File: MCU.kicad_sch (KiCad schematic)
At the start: 13 parts, among them J7 USB_C_Receptacle_USB2.0_16P, U1 STM32G474RCTx

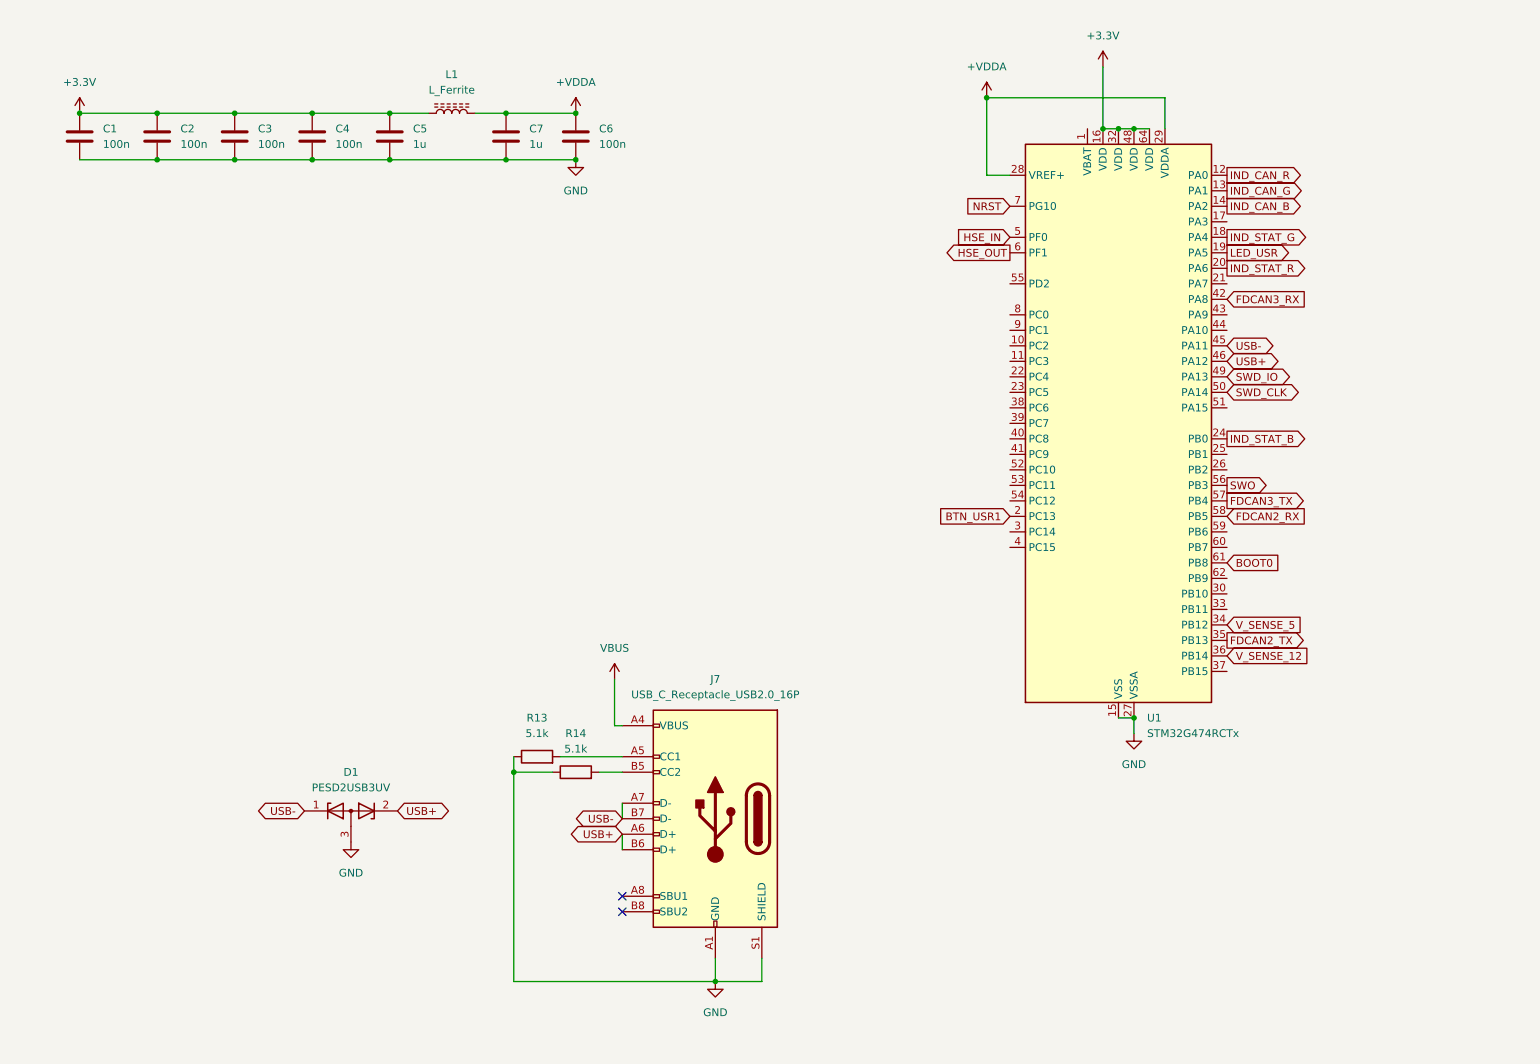
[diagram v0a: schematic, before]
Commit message: add power, some mcu components
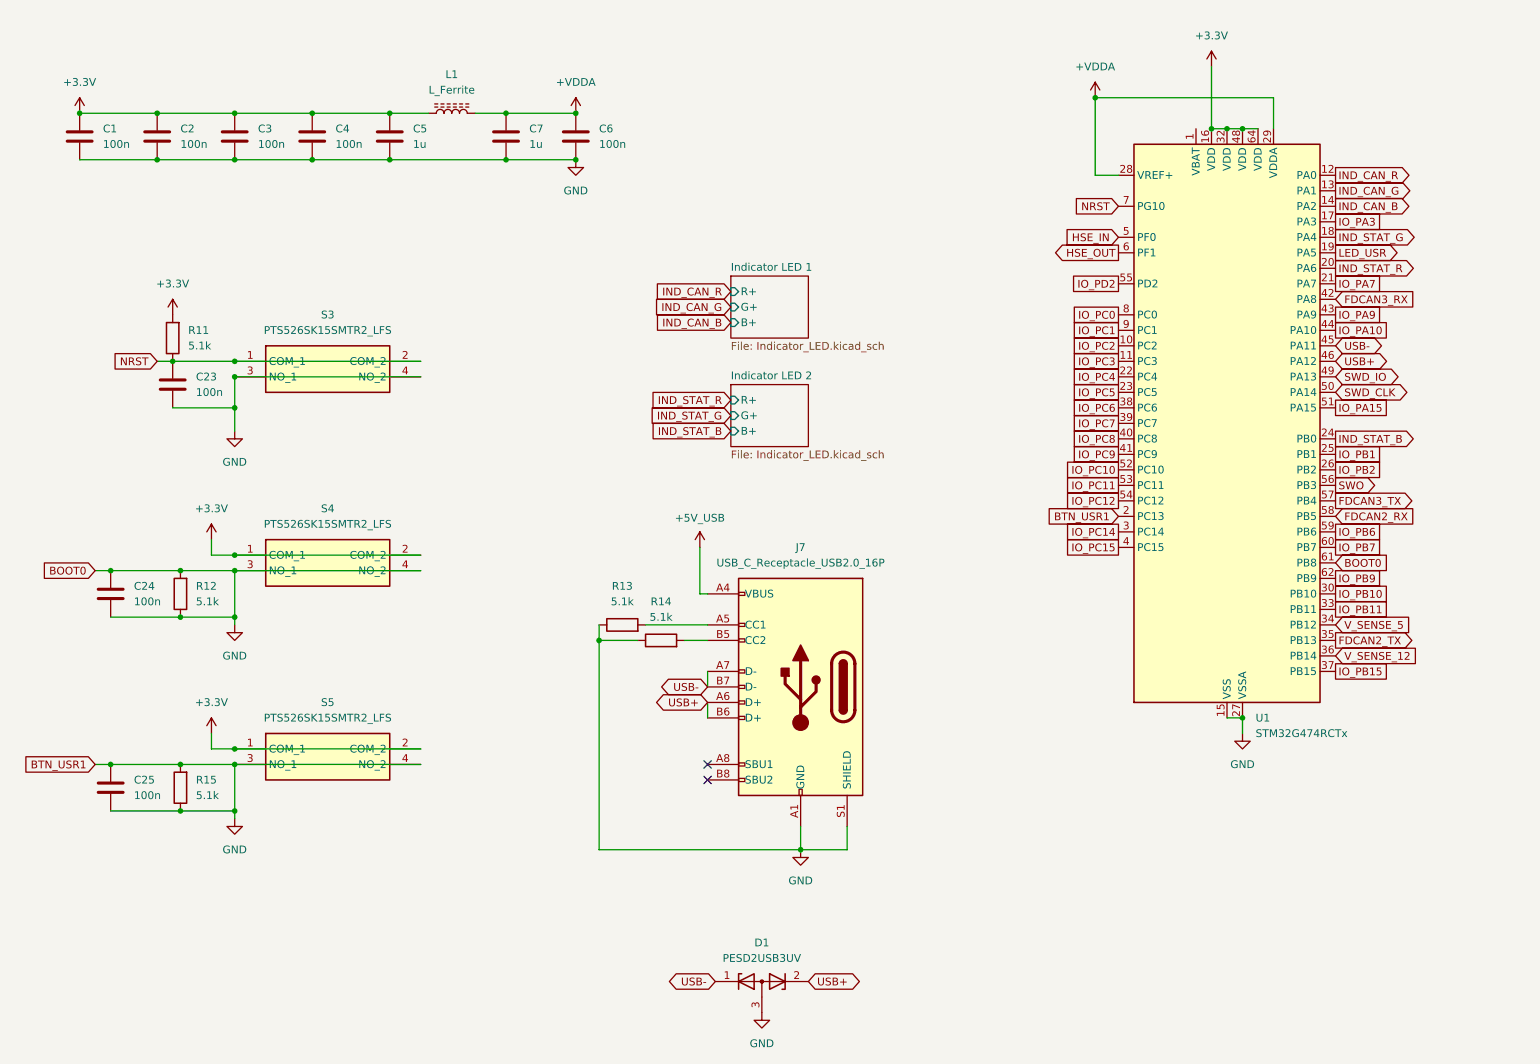
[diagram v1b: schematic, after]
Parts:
- added C23, C24, C25: 100n, Capacitor_SMD:C_0603_1608Metric_Pad1.08x0.95mm_HandSolder, symbol Device:C
- added R11, R12, R15: 5.1k, Resistor_SMD:R_0603_1608Metric_Pad0.98x0.95mm_HandSolder, symbol Device:R
- added S3, S4, S5: PTS526SK15SMTR2_LFS, PTS526SK15SMTR2LFS, symbol SamacSys_Parts:PTS526SK15SMTR2_LFS
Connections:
- net BOOT0 is gone; now on net GND: U1.61 (PB8)
- net BTN_USR1 is gone; now on net GND: U1.2 (PC13)
- net +3.3V: now also R11.2, S4.1 (COM_1), S4.2 (COM_2), S5.1 (COM_1), S5.2 (COM_2)
- net GND: now also C23.2, C24.1, C24.2, C25.1, C25.2, R12.1, R12.2, R15.1, R15.2, S3.3 (NO_1), S3.4 (NO_2), S4.3 (NO_1), S4.4 (NO_2), S5.3 (NO_1), S5.4 (NO_2)
- net NRST: now also C23.1, R11.1, S3.1 (COM_1), S3.2 (COM_2)
- net IO_PC2: now reaches U1.10 (PC2)
- net IO_PC3: now reaches U1.11 (PC3)
- net IO_PA3: now reaches U1.17 (PA3)
- net IO_PA7: now reaches U1.21 (PA7)
- net IO_PC4: now reaches U1.22 (PC4)
- net IO_PC5: now reaches U1.23 (PC5)
- net IO_PB1: now reaches U1.25 (PB1)
- net IO_PB2: now reaches U1.26 (PB2)
- net IO_PC14: now reaches U1.3 (PC14)
- net IO_PB10: now reaches U1.30 (PB10)
- net IO_PB11: now reaches U1.33 (PB11)
- net IO_PB15: now reaches U1.37 (PB15)
- net IO_PC6: now reaches U1.38 (PC6)
- net IO_PC7: now reaches U1.39 (PC7)
- net IO_PC15: now reaches U1.4 (PC15)
- net IO_PC8: now reaches U1.40 (PC8)
- net IO_PC9: now reaches U1.41 (PC9)
- net IO_PA9: now reaches U1.43 (PA9)
- net IO_PA10: now reaches U1.44 (PA10)
- net IO_PA15: now reaches U1.51 (PA15)
- net IO_PC10: now reaches U1.52 (PC10)
- net IO_PC11: now reaches U1.53 (PC11)
- net IO_PC12: now reaches U1.54 (PC12)
- net IO_PD2: now reaches U1.55 (PD2)
- net IO_PB6: now reaches U1.59 (PB6)
- net IO_PB7: now reaches U1.60 (PB7)
- net IO_PB9: now reaches U1.62 (PB9)
- net IO_PC0: now reaches U1.8 (PC0)
- net IO_PC1: now reaches U1.9 (PC1)
- net VBUS renamed +5V_USB
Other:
- added sheet Indicator LED 1 (Indicator_LED.kicad_sch)
- added sheet Indicator LED 2 (Indicator_LED.kicad_sch)
- moved on the sheet: D1, J7, R13, R14, U1

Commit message: complete schematic, initial board layout
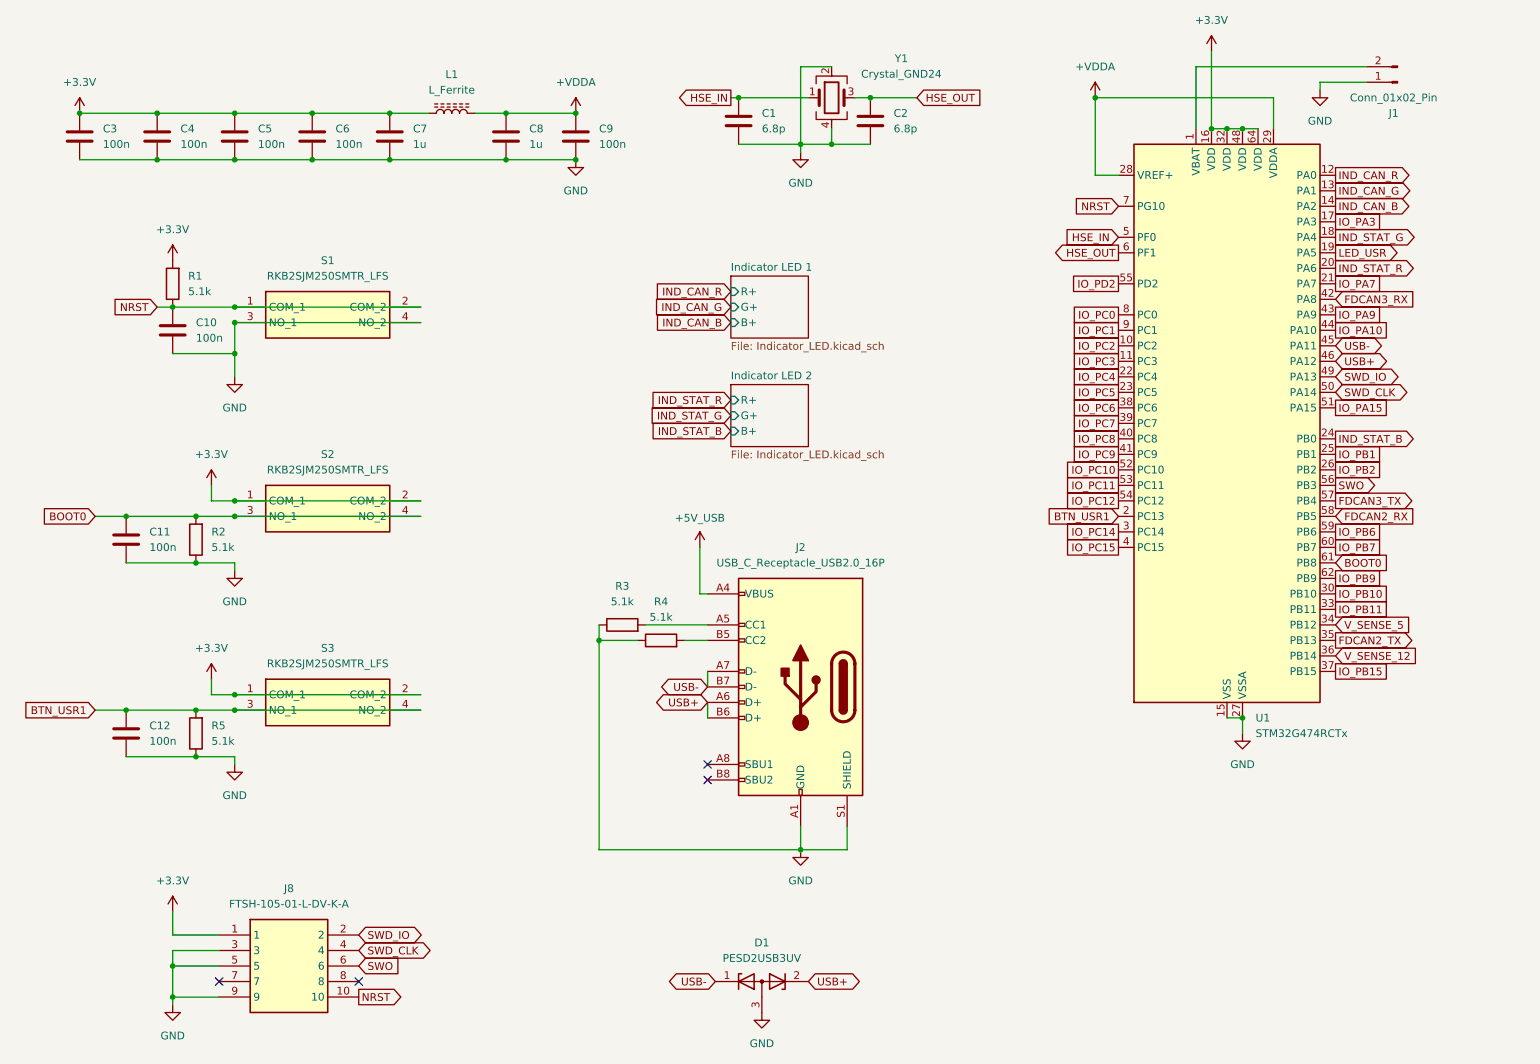
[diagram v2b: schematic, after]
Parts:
- removed S3, S4, S5: PTS526SK15SMTR2_LFS, PTS526SK15SMTR2LFS, symbol SamacSys_Parts:PTS526SK15SMTR2_LFS
- added C1, C2: 6.8p, Capacitor_SMD:C_0603_1608Metric_Pad1.08x0.95mm_HandSolder, symbol Device:C
- added J1: Conn_01x02_Pin, Connector_PinHeader_2.54mm:PinHeader_1x02_P2.54mm_Vertical, symbol Connector:Conn_01x02_Pin
- added J8: FTSH-105-01-L-DV-K-A, SamacSys_Parts:FTSH-105-XX-YYY-DV-K-A, symbol SamacSys_Parts:FTSH-105-01-L-DV-K-A
- added S1, S2, S3: RKB2SJM250SMTR_LFS, RKB2SJM250SMTRLFS, symbol SamacSys_Parts:RKB2SJM250SMTR_LFS
- added Y1: Crystal_GND24, Crystal:Crystal_SMD_3225-4Pin_3.2x2.5mm, symbol Device:Crystal_GND24
- renumbered C23 to C10, C24 to C11, C25 to C12, C1 to C3, C2 to C4, C3 to C5, C4 to C6, C5 to C7, C7 to C8, C6 to C9, J7 to J2, R11 to R1, R12 to R2, R13 to R3, R14 to R4, R15 to R5
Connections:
- net +3.3V: now also J8.1, S2.1 (COM_1), S2.2 (COM_2), S3.1 (COM_1), S3.2 (COM_2)
- net GND: now also C1.2, C2.2, J1.1 (Pin_1), J8.3, J8.5, J8.9, S1.3 (NO_1), S1.4 (NO_2), Y1.2, Y1.4; no longer C11.1, C12.1, R2.2, R5.2, U1.2 (PC13), U1.61 (PB8)
- net HSE_IN: now also C1.1, Y1.1
- net HSE_OUT: now also C2.1, Y1.3
- net NRST: now also J8.10, S1.1 (COM_1), S1.2 (COM_2)
- net SWD_CLK: now also J8.4
- net SWD_IO: now also J8.2
- net SWO: now also J8.6
- net at U1.1 (VBAT): now also J1.2 (Pin_2)
- new net BOOT0: C11.1, R2.2, S2.3 (NO_1), S2.4 (NO_2), U1.61 (PB8)
- new net BTN_USR1: C12.1, R5.2, S3.3 (NO_1), S3.4 (NO_2), U1.2 (PC13)
- no-connect marks 2 -> 4
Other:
- moved on the sheet: C10, C11, C12, R1, R2, R5

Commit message: layout almost complete
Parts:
- added D9: LED, LED_SMD:LED_0603_1608Metric_Pad1.05x0.95mm_HandSolder, symbol Device:LED
- added R21: 470, Resistor_SMD:R_0603_1608Metric_Pad0.98x0.95mm_HandSolder, symbol Device:R
- D1: footprint Package_TO_SOT_SMD:SOT-23_Handsoldering -> Package_TO_SOT_SMD:SOT-23W
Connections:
- net GND: now also D9.1 (K)
- net LED_USR: now also R21.1
- new net: D9.2 (A), R21.2

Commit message: completed layout and routing
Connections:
- net LED_USR renamed IO_PA5
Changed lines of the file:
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@@
+	)
+	(junction
+		(at 259.08 68.58)
+		(diameter 0)
+		(color 0 0 0 0)
 	)
 	(junction
@@
 	)
 	(junction
+		(at 259.08 101.6)
+		(diameter 0)
+		(color 0 0 0 0)
+	)
+	(junction
 		(at 63.5 72.39)
 		(diameter 0)
@@
 	(junction
 		(at 63.5 45.72)
+		(diameter 0)
+		(color 0 0 0 0)
+	)
+	(junction
+		(at 259.08 60.96)
 		(diameter 0)
 		(color 0 0 0 0)
@@
 	(wire
 		(pts
+			(xy 259.08 101.6) (xy 243.84 101.6)
+		)
+		(stroke
+			(width 0)
+			(type default)
+		)
+	)
+	(wire
+		(pts
+			(xy 259.08 100.33) (xy 259.08 101.6)
+		)
+		(stroke
+			(width 0)
+			(type default)
+		)
+	)
+	(wire
+		(pts
 			(xy 123.19 124.46) (xy 129.54 124.46)
 		)
@@
 	(wire
 		(pts
+			(xy 260.35 100.33) (xy 259.08 100.33)
+		)
+		(stroke
+			(width 0)
+			(type default)
+		)
+	)
+	(wire
+		(pts
 			(xy 38.1 45.72) (xy 50.8 45.72)
 		)
@@
 	(wire
 		(pts
+			(xy 260.35 67.31) (xy 259.08 67.31)
+		)
+		(stroke
+			(width 0)
+			(type default)
+		)
+	)
+	(wire
+		(pts
 			(xy 53.34 77.47) (xy 63.5 77.47)
 		)
@@
 	(wire
 		(pts
+			(xy 260.35 62.23) (xy 259.08 62.23)
+		)
+		(stroke
+			(width 0)
+			(type default)
+		)
+	)
+	(wire
+		(pts
 			(xy 63.5 38.1) (xy 76.2 38.1)
 		)
@@
 	(wire
 		(pts
+			(xy 259.08 102.87) (xy 259.08 101.6)
+		)
+		(stroke
+			(width 0)
+			(type default)
+		)
+	)
+	(wire
+		(pts
 			(xy 226.06 40.64) (xy 223.52 40.64)
 		)
@@
 	(wire
 		(pts
+			(xy 260.35 69.85) (xy 259.08 69.85)
+		)
+		(stroke
+			(width 0)
+			(type default)
+		)
+	)
+	(wire
+		(pts
 			(xy 167.64 35.56) (xy 165.1 35.56)
 		)
@@
 	(wire
 		(pts
+			(xy 259.08 68.58) (xy 243.84 68.58)
+		)
+		(stroke
+			(width 0)
+			(type default)
+		)
+	)
+	(wire
+		(pts
+			(xy 260.35 102.87) (xy 259.08 102.87)
+		)
+		(stroke
+			(width 0)
+			(type default)
+		)
+	)
+	(wire
+		(pts
 			(xy 204.47 48.26) (xy 208.28 48.26)
 		)
@@
 	(wire
 		(pts
+			(xy 259.08 60.96) (xy 243.84 60.96)
+		)
+		(stroke
+			(width 0)
+			(type default)
+		)
+	)
+	(wire
+		(pts
 			(xy 167.64 43.18) (xy 161.29 43.18)
 		)
@@
 	(wire
 		(pts
+			(xy 259.08 69.85) (xy 259.08 68.58)
+		)
+		(stroke
+			(width 0)
+			(type default)
+		)
+	)
+	(wire
+		(pts
 			(xy 123.19 121.92) (xy 123.19 124.46)
 		)
@@
 	(wire
 		(pts
+			(xy 259.08 67.31) (xy 259.08 68.58)
+		)
+		(stroke
+			(width 0)
+			(type default)
+		)
+	)
+	(wire
+		(pts
 			(xy 204.47 35.56) (xy 204.47 48.26)
 		)
@@
 	(wire
 		(pts
+			(xy 260.35 59.69) (xy 259.08 59.69)
+		)
+		(stroke
+			(width 0)
+			(type default)
+		)
+	)
+	(wire
+		(pts
 			(xy 233.68 35.56) (xy 204.47 35.56)
 		)
@@
 	(wire
 		(pts
+			(xy 259.08 60.96) (xy 259.08 62.23)
+		)
+		(stroke
+			(width 0)
+			(type default)
+		)
+	)
+	(wire
+		(pts
 			(xy 59.69 133.35) (xy 63.5 133.35)
 		)
@@
 		)
 	)
+	(wire
+		(pts
+			(xy 259.08 59.69) (xy 259.08 60.96)
+		)
+		(stroke
+			(width 0)
+			(type default)
+		)
+	)
 	(global_label "IO_PD2"
 		(shape passive)
@@
 				)
 				(justify right)
+				(hide yes)
+			)
+		)
+	)
+	(global_label "IO_PA5"
+		(shape passive)
+		(at 260.35 62.23 0)
+		(fields_autoplaced yes)
+		(effects
+			(font
+				(size 1.27 1.27)
+				(color 0 0 132 1)
+			)
+			(justify left)
+		)
+		(property "Intersheetrefs" "${INTERSHEET_REFS}"
+			(at 268.6949 62.23 0)
+			(effects
+				(font
+					(size 1.27 1.27)
+				)
+				(justify left)
 				(hide yes)
 			)
@@
 	(global_label "LED_USR"
 		(shape output)
-		(at 243.84 60.96 0)
-		(fields_autoplaced yes)
-		(effects
-			(font
-				(size 1.27 1.27)
-			)
-			(justify left)
-		)
-		(property "Intersheetrefs" "${INTERSHEET_REFS}"
-			(at 255.0499 60.96 0)
+		(at 260.35 59.69 0)
+		(fields_autoplaced yes)
+		(effects
+			(font
+				(size 1.27 1.27)
+			)
+			(justify left)
+		)
+		(property "Intersheetrefs" "${INTERSHEET_REFS}"
+			(at 271.5599 59.69 0)
 			(effects
 				(font
@@
 	(global_label "FDCAN3_TX"
 		(shape output)
-		(at 243.84 101.6 0)
-		(fields_autoplaced yes)
-		(effects
-			(font
-				(size 1.27 1.27)
-			)
-			(justify left)
-		)
-		(property "Intersheetrefs" "${INTERSHEET_REFS}"
-			(at 257.2271 101.6 0)
+		(at 260.35 100.33 0)
+		(fields_autoplaced yes)
+		(effects
+			(font
+				(size 1.27 1.27)
+			)
+			(justify left)
+		)
+		(property "Intersheetrefs" "${INTERSHEET_REFS}"
+			(at 273.7371 100.33 0)
 			(effects
 				(font
@@
 	(global_label "FDCAN3_RX"
 		(shape input)
-		(at 243.84 68.58 0)
-		(fields_autoplaced yes)
-		(effects
-			(font
-				(size 1.27 1.27)
-			)
-			(justify left)
-		)
-		(property "Intersheetrefs" "${INTERSHEET_REFS}"
-			(at 257.5295 68.58 0)
+		(at 260.35 67.31 0)
+		(fields_autoplaced yes)
+		(effects
+			(font
+				(size 1.27 1.27)
+			)
+			(justify left)
+		)
+		(property "Intersheetrefs" "${INTERSHEET_REFS}"
+			(at 274.0395 67.31 0)
 			(effects
 				(font
@@
 		)
 	)
+	(global_label "IO_PA8"
+		(shape passive)
+		(at 260.35 69.85 0)
+		(fields_autoplaced yes)
+		(effects
+			(font
+				(size 1.27 1.27)
+				(color 0 0 132 1)
+			)
+			(justify left)
+		)
+		(property "Intersheetrefs" "${INTERSHEET_REFS}"
+			(at 268.6949 69.85 0)
+			(effects
+				(font
+					(size 1.27 1.27)
+				)
+				(justify left)
+				(hide yes)
+			)
+		)
+	)
 	(global_label "USB+"
 		(shape bidirectional)
@@
 			(effects
 				(font
+					(size 1.27 1.27)
+				)
+				(justify left)
+				(hide yes)
+			)
+		)
+	)
+	(global_label "IO_PB4"
+		(shape passive)
+		(at 260.35 102.87 0)
+		(fields_autoplaced yes)
+		(effects
+			(font
+				(size 1.27 1.27)
+				(color 0 0 132 1)
+			)
+			(justify left)
+		)
+		(property "Intersheetrefs" "${INTERSHEET_REFS}"
+			(at 268.8763 102.87 0)
+			(effects
+				(font
